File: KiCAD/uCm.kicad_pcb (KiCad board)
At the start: 2 copper layers, 99 x 80 mm, 156 parts, among them J1 5V_EXT, J2 3V3_EXT, P1 AREF, P10 C3SB, P11 VSel_Vlv, P13 PWR_IN, P14 X_VALVE, P17 PUMP, P24 PWR_IN, P34 VSel_Vlv2, P38 X_VALVE2, P4 ICSP, P5 FTDI, P7 GAGE_PR, P9 C3SB, Q1 BCP5416TA, Q2 BCP5416TA, Q3 BCP5416TA, Q4 BCP5416TA, SW1 Reset, SW2 INT0, SW3 INT1, U1 TXB0104D, U3 TPS62133, U4 TPS62132, U5 DS3231N, U7 ATMEGA328-AU-ND, X1 16MHz

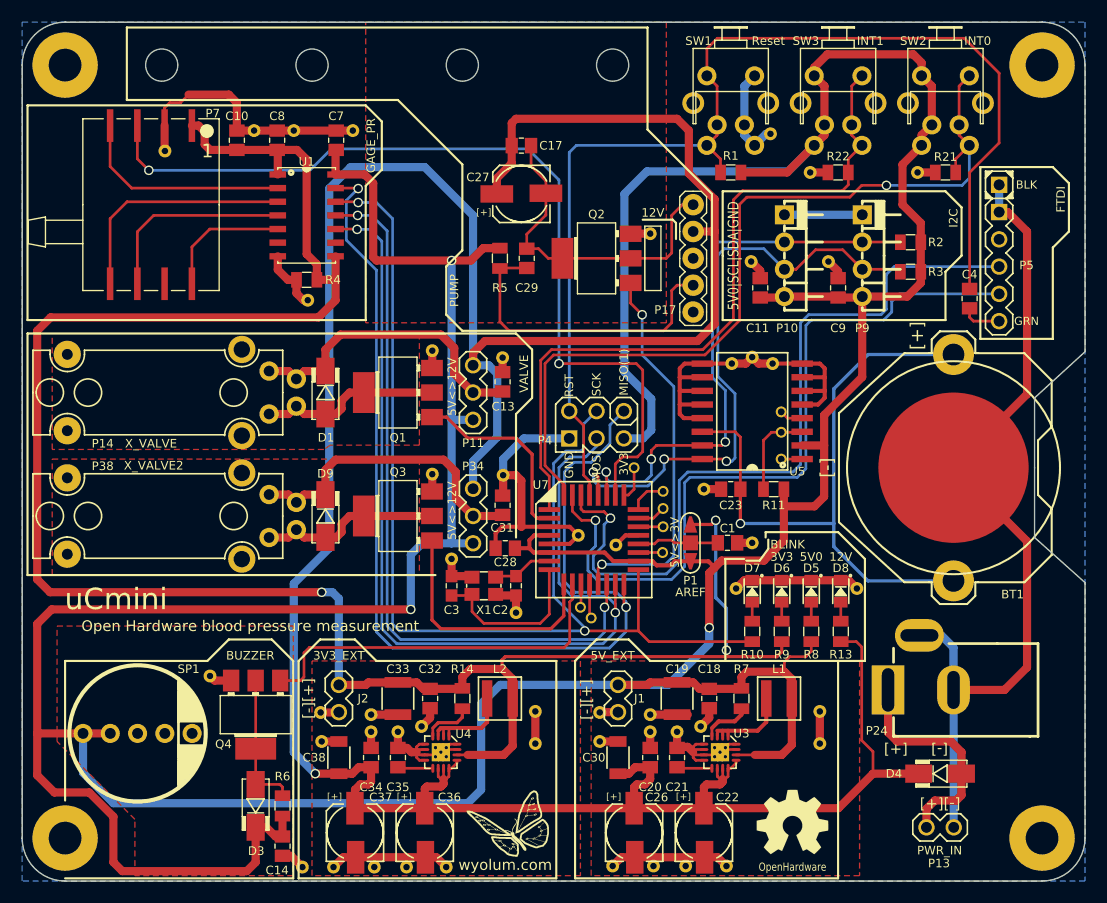
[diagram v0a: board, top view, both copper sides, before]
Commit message: power supply sections changed
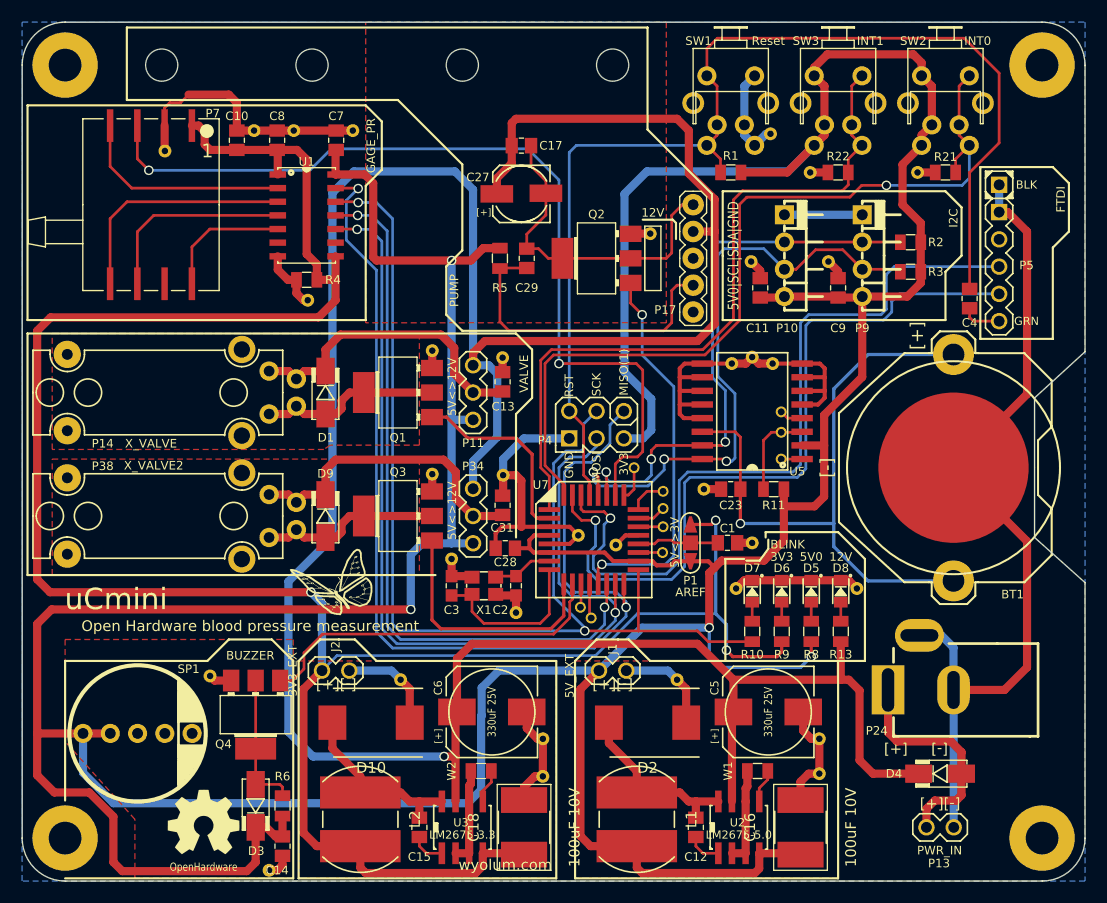
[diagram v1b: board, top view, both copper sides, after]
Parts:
- removed C19, C33: 22uF X7R, uCm:C_1210
- removed C20, C32, C34: 100nF, uCm:c_0805
- removed C21, C35: 3.3nF, uCm:c_0805
- removed C22, C26, C36, C37: 100uF, uCm:C_ELCO_SMD
- removed C30, C38: 10uF X7R, uCm:C_1206
- removed R14, R7: 100k, uCm:r_0805
- removed the REF** at (67.8, 78.3)
- removed the REF** at (46.8, 92.7)
- removed the REF** at (51.2, 79.6)
- removed the REF** at (41.9, 81.0)
- removed the REF** at (49.0, 80.1)
- removed the REF** at (46.5, 78.5)
- removed the REF** at (46.5, 80.1)
- removed the REF** at (88.3, 78.2)
- removed the REF** at (88.3, 81.2)
- removed the REF** at (61.8, 81.2)
- removed the REF** at (61.8, 78.2)
- removed the REF** at (77.2, 79.6)
- removed the REF** at (75.0, 80.1)
- removed the REF** at (53.5, 92.7)
- removed the REF** at (79.6, 92.6)
- removed the REF** at (69.0, 92.6)
- removed the REF** at (72.5, 78.5)
- removed the REF** at (41.8, 78.3)
- removed the REF** at (43.0, 92.7)
- removed the REF** at (40.1, 92.7)
- removed the REF** at (72.5, 80.1)
- removed the REF** at (67.8, 81.0)
- removed the REF** at (75.8, 92.6)
- removed the REF** at (72.8, 92.6)
- removed the REF** at (49.8, 92.7)
- removed U4: TPS62132, uCm:TPS62132
- added C12: 10nF, uCm:c_0805, F.Cu at (76.8, 89.0)
- added C15: 10nF, uCm:c_0805, F.Cu at (51.0, 89.0)
- added C16: 100uF 10V, uCm:C_2917_HandSoldering, F.Cu at (86.5, 89.0)
- added C5: 330uF 25V, uCm:C_ELCO_SMD_8x10, F.Cu at (83.5, 78.2)
- added C6: 330uF 25V, uCm:C_ELCO_SMD_8x10, F.Cu at (57.8, 78.2)
- added D10: SS35, uCm:DO-214AB, F.Cu at (46.5, 79.2)
- added D2: SS35, uCm:DO-214AB, F.Cu at (72.2, 79.2)
- added REF**: via01, uCm:via01, F.Cu at (37.0, 93.0)
- added REF**: via01, uCm:via01, F.Cu at (88.2, 84.0)
- added REF**: via01, uCm:via01, F.Cu at (88.2, 80.8)
- added REF**: via01, uCm:via01, F.Cu at (49.2, 75.2)
- added REF**: via01, uCm:via01, F.Cu at (62.5, 84.2)
- added REF**: via01, uCm:via01, F.Cu at (75.0, 75.2)
- added REF**: via01, uCm:via01, F.Cu at (62.5, 80.8)
- added U2: LM2675-5.0, uCm:SO8E, F.Cu at (80.8, 89.0)
- added W1: EN, uCm:r_0805, F.Cu at (82.5, 83.8)
- added W2: EN, uCm:r_0805, F.Cu at (56.8, 83.8)
- C1, C4: value 100nF -> 100n
- C18: value 100nF -> 100uF 10V; footprint uCm:c_0805 -> uCm:C_2917_HandSoldering
- D1, D3, D4, D9: value S1D-13-F -> ES1D-13-F
- L1, L2: value 2u2H,3.0A -> 33uH; footprint uCm:Inductor_SMD3 -> uCm:Choke_SMD_Wuerth-784775133
- U3: value TPS62133 -> LM2675-3.3; footprint uCm:TPS62132 -> uCm:SO8E
- moved G3 54.9 mm to (30.9, 88.5)
- moved G2 27.9 mm to (37.8, 62.5)
- moved U3 25.0 mm to (55.0, 89.0), turned to 0 degrees
- moved C18 21.0 mm to (60.8, 89.0), turned to 90 degrees
- moved L1 17.4 mm to (71.2, 88.2), turned to 270 degrees
- moved L2 17.2 mm to (45.5, 88.2), turned to 270 degrees
- moved J1 2.65 mm to (69.0, 74.4), turned to 0 degrees
- moved J2 2.62 mm to (43.2, 74.4), turned to 0 degrees
- turned C4 to 90 degrees
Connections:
- C18 pad 1: GND -> +3.3V
- C18 pad 2: /Interface/5V0 -> GND
- C4 pad 1: /~RTS -> /RESET
- C4 pad 2: /RESET -> /~RTS
- L1 pad 1: Net-(L1-Pad1) -> /pwr/VSW5
- L2 pad 1: Net-(L2-Pad1) -> /pwr/VSW3
- U3 pad 1: Net-(L1-Pad1) -> /pwr/CB3
- U3 pad 2: Net-(L1-Pad1) -> GND
- U3 pad 3: Net-(L1-Pad1) -> GND
- U3 pad 4: Net-(R7-Pad1) -> +3.3V
- U3 pad 5: GND -> Net-(U3-Pad5)
- U3 pad 7: GND -> /Interface/12V
- U3 pad 8: GND -> /pwr/VSW3
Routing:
- net +3.3V: track 195.3 -> 219.3 mm
- net GND: track 315.7 -> 293.7 mm
- net /Interface/5V0: track 443.7 -> 464.4 mm, vias 3 -> 4
- net /pwr/VSW3: track 0.00 -> 17.0 mm
- net /pwr/VSW5: track 0.00 -> 17.0 mm
- net /Interface/12V: track 275.9 -> 264.4 mm
- net Net-(L2-Pad1): track 9.09 -> 0.00 mm
- net Net-(L1-Pad1): track 8.59 -> 0.00 mm
- net Net-(R14-Pad1): track 4.71 -> 0.00 mm
- net Net-(R7-Pad1): track 4.57 -> 0.00 mm
- net Net-(C21-Pad2): track 3.29 -> 0.00 mm
- net Net-(C35-Pad2): track 3.29 -> 0.00 mm
- net /pwr/CB5: track 0.00 -> 3.22 mm
- net /pwr/CB3: track 0.00 -> 3.22 mm
- net Net-(U3-Pad5): track 0.00 -> 3.17 mm
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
